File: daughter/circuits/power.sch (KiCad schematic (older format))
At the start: 44 parts, among them J5 Barrel_Jack_OD5.5_ID2.5, J6 Barrel_Jack_OD5.5_ID2.5, J7 Barrel_Jack_OD5.5_ID2.5, U2 LTV-827S, U3 ACS711, U4 REG_3V3, U5 MIC29302WU, U6 MIC29302WU, U7 MIC29302WU

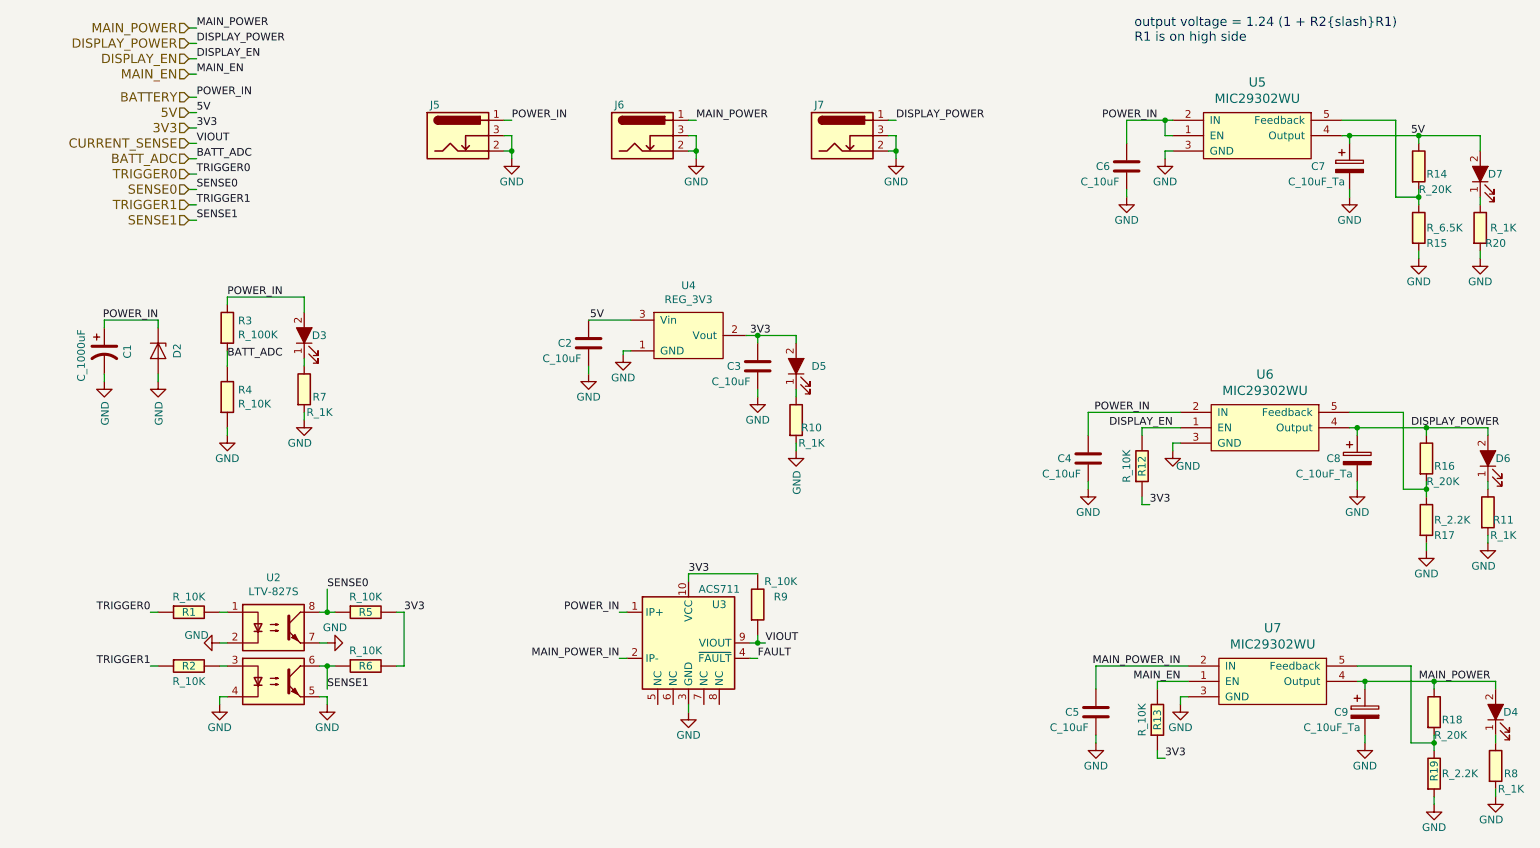
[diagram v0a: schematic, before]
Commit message: 0) Switched to h-bridge drivers for hvac 1) Connected ignition sense io 2) MCP config pins and reset 3) Fixed usb resistors 4) Fixed BJT footprint 5) Added car interface pcb for C6 Corvette
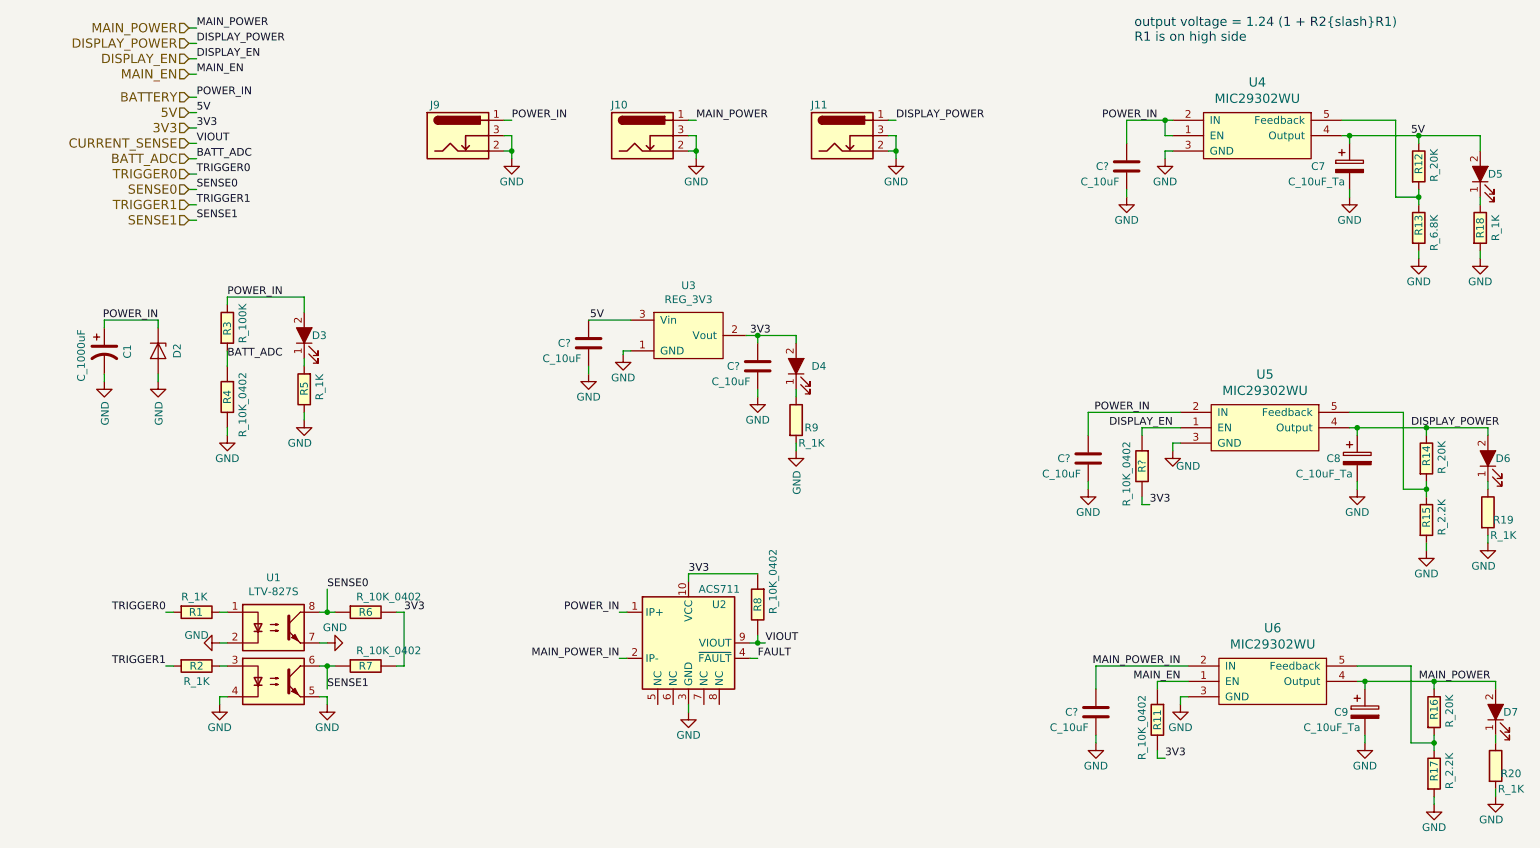
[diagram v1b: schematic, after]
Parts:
- removed C2, C3, C4, C5, C6: C_10uF, Capacitor_SMD:C_0603_1608Metric_Pad1.08x0.95mm_HandSolder, symbol open-dash-daughterboard-rescue:C_10uF-Open_Automation
- removed R1, R12, R13, R2, R4, R5, R6, R9: R_10K, Resistor_SMD:R_0603_1608Metric_Pad0.98x0.95mm_HandSolder, symbol open-dash-daughterboard-rescue:R_10K-Open_Automation
- removed R14, R16, R18: R_20K, Resistor_SMD:R_0603_1608Metric_Pad0.98x0.95mm_HandSolder, symbol open-dash-daughterboard-rescue:R_20K-Open_Automation
- removed R15: R_6.5K, Resistor_SMD:R_0603_1608Metric_Pad0.98x0.95mm_HandSolder, symbol open-dash-daughterboard-rescue:R_6.5K-Open_Automation
- removed R17, R19: R_2.2K, Resistor_SMD:R_0603_1608Metric_Pad0.98x0.95mm_HandSolder, symbol open-dash-daughterboard-rescue:R_2.2K-Open_Automation
- removed R3: R_100K, Resistor_SMD:R_0603_1608Metric_Pad0.98x0.95mm_HandSolder, symbol open-dash-daughterboard-rescue:R_100K-Open_Automation
- removed R7, R8: R_1K, Resistor_SMD:R_0603_1608Metric_Pad0.98x0.95mm_HandSolder, symbol open-dash-daughterboard-rescue:R_1K-Open_Automation
- removed U5: MIC29302WU, Package_TO_SOT_SMD:TO-263-5_TabPin3, symbol open-dash-daughterboard-rescue:MIC29302WU-Open_Automation
- added C? (x5): C_10uF, Capacitor_SMD:C_0805_2012Metric_Pad1.18x1.45mm_HandSolder, symbol Open_Automation:C_10uF
- added R1, R2, R5: R_1K, Resistor_SMD:R_0603_1608Metric_Pad0.98x0.95mm_HandSolder, symbol Open_Automation:R_1K
- added R11, R4, R6, R7, R8, R?: R_10K_0402, Resistor_SMD:R_0402_1005Metric_Pad0.72x0.64mm_HandSolder, symbol Open_Automation:R_10K_0402
- added R12, R14, R16: R_20K, Resistor_SMD:R_0402_1005Metric_Pad0.72x0.64mm_HandSolder, symbol Open_Automation:R_20K
- added R13: R_6.8K, Resistor_SMD:R_0603_1608Metric_Pad0.98x0.95mm_HandSolder, symbol Open_Automation:R_6.8K
- added R15, R17: R_2.2K, Resistor_SMD:R_0402_1005Metric_Pad0.72x0.64mm_HandSolder, symbol Open_Automation:R_2.2K
- added R20: R_1K, Resistor_SMD:R_0603_1608Metric_Pad0.98x0.95mm_HandSolder, symbol open-dash-daughterboard-rescue:R_1K-Open_Automation
- added R3: R_100K, Resistor_SMD:R_0603_1608Metric_Pad0.98x0.95mm_HandSolder, symbol Open_Automation:R_100K
- added U4: MIC29302WU, Package_TO_SOT_SMD:TO-263-5_TabPin3, symbol open-dash-daughterboard-rescue:MIC29302WU-Open_Automation
- renumbered D5 to D4, D7 to D5, D4 to D7, J6 to J10, J7 to J11, J5 to J9, R20 to R18, R11 to R19, R10 to R9, U2 to U1, U3 to U2, U4 to U3, U6 to U5, U7 to U6
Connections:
- net 3V3: now also C?.1, R11.2, R6.2, R7.2, R8.1, R?.2
- net 5V: now also C?.1, R12.1, U4.4 (Output)
- net BATTERY: now also C?.1, C?.1, R3.1, U4.1 (EN), U4.2 (IN)
- net BATT_ADC: now also R3.2, R4.1
- net CURRENT_SENSE: now also R8.2
- net DISPLAY_EN: now also R?.1
- net DISPLAY_POWER: now also R14.1
- net GND: now also C?.2, C?.2, C?.2, C?.2, C?.2, R13.2, R15.2, R17.2, R20.2, R4.2, R5.1, U4.3 (GND)
- net MAIN_EN: now also R11.1
- net MAIN_POWER: now also R16.1
- net MAIN_POWER_IN: now also C?.1
- net SENSE0: now also R6.1
- net SENSE1: now also R7.1
- net TRIGGER0: now also R1.2
- net TRIGGER1: now also R2.2
- net at U5.5 (Feedback): now also R14.2, R15.1
- net at U6.5 (Feedback): now also R16.2, R17.1
- net at D3.1 (K): now also R5.2
- net at D7.1 (K): now also R20.1
- net at U1.1: now also R1.1
- net at U1.3: now also R2.1
- new net: R12.2, R13.1, U4.5 (Feedback)

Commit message: finished schematic, working on layout
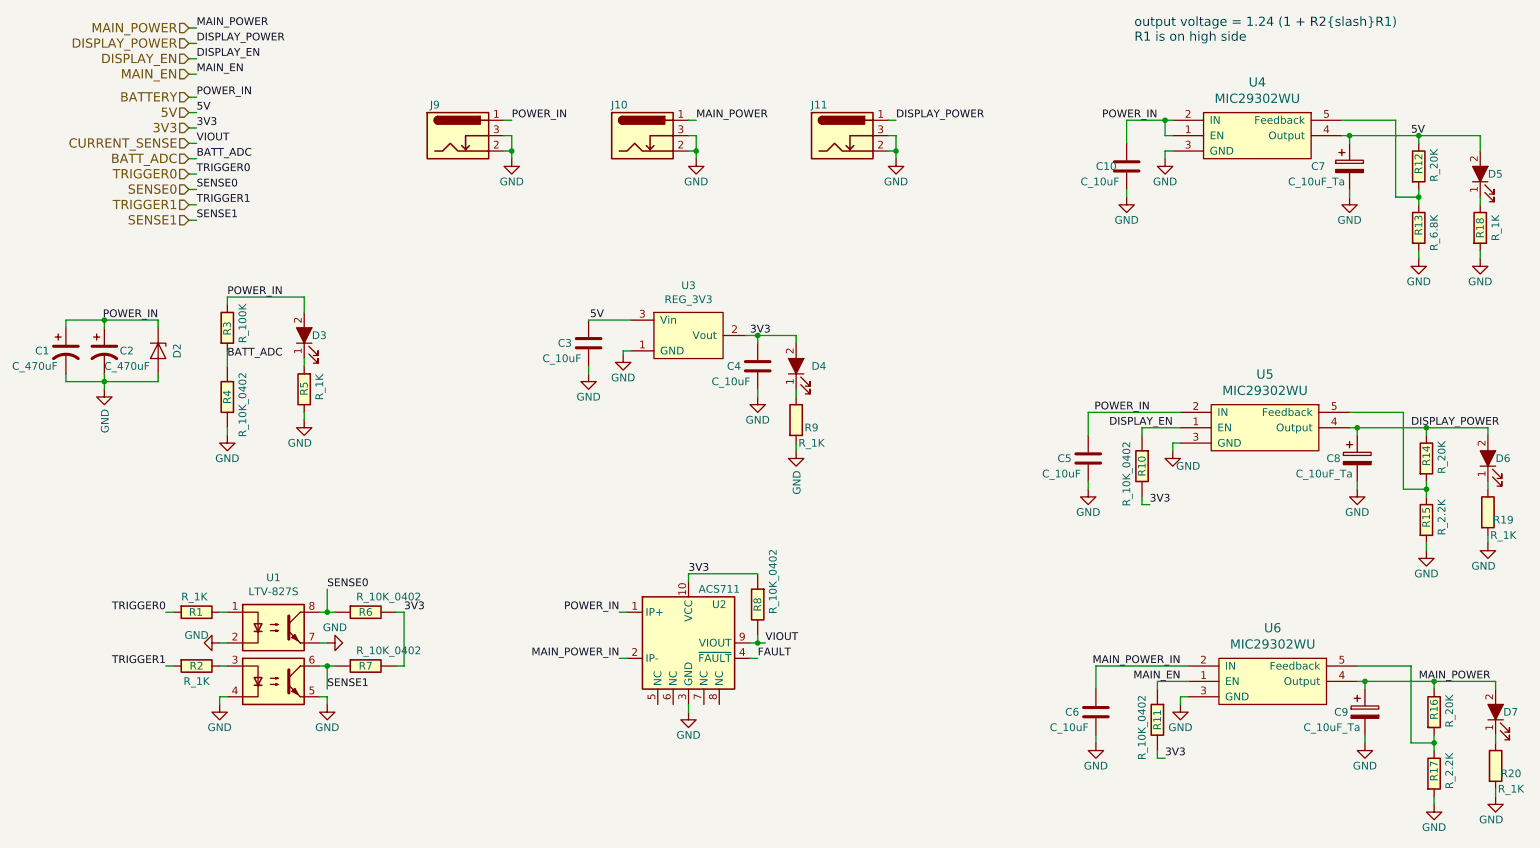
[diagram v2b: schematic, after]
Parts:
- removed C1: C_1000uF, Capacitor_THT:CP_Radial_D12.5mm_P5.00mm, symbol open-dash-daughterboard-rescue:C_1000uF-Open_Automation
- added C1, C2: C_470uF, Capacitor_SMD:CP_Elec_10x10, symbol Open_Automation:C_470uF
- gave numbers to parts that had none: 6
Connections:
- net BATTERY: now also C1.1, C2.1
- net GND: now also C1.2, C2.2
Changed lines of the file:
@@
 L open-dash-daughterboard-rescue:GND-power #PWR025
 U 1 1 5FD22FE0
-P 1150 3350
-F 0 "#PWR025" H 1150 3100 50  0001 C CNN
-F 1 "GND" V 1155 3222 50  0000 R CNN
-F 2 "" H 1150 3350 50  0001 C CNN
-F 3 "" H 1150 3350 50  0001 C CNN
-	1    1150 3350
-	1    0    0    -1
-$EndComp
-$Comp
-L open-dash-daughterboard-rescue:GND-power #PWR026
-U 1 1 5FD22FD6
-P 1500 3350
-F 0 "#PWR026" H 1500 3100 50  0001 C CNN
-F 1 "GND" V 1505 3222 50  0000 R CNN
-F 2 "" H 1500 3350 50  0001 C CNN
-F 3 "" H 1500 3350 50  0001 C CNN
-	1    1500 3350
+P 1150 3400
+F 0 "#PWR025" H 1150 3150 50  0001 C CNN
+F 1 "GND" V 1155 3272 50  0000 R CNN
+F 2 "" H 1150 3400 50  0001 C CNN
+F 3 "" H 1150 3400 50  0001 C CNN
+	1    1150 3400
 	1    0    0    -1
 $EndComp
@@
 F 3 "" H 4525 3175 50  0000 C CNN
 	1    4525 3175
-	1    0    0    -1
-$EndComp
-$Comp
-L open-dash-daughterboard-rescue:C_1000uF-Open_Automation C?
-U 1 1 5CC3872E
-P 1150 3150
-AR Path="/5ABD18ED/5CC3872E" Ref="C?"  Part="1"
-AR Path="/5CC3872E" Ref="C?"  Part="1"
-AR Path="/5A7BADB8/5CC3872E" Ref="C1"  Part="1"
-F 0 "C1" V 1300 3100 50  0000 L CNN
-F 1 "C_1000uF" V 1000 2950 50  0000 L CNN
-F 2 "Capacitor_THT:CP_Radial_D12.5mm_P5.00mm" H 1250 3450 50  0001 C CNN
-F 3 "https://industrial.panasonic.com/ww/products/capacitors/aluminum-capacitors/aluminum-cap-lead/fc/EEUFC1E102" H 1150 2900 50  0001 C CNN
-F 4 " EEU-FC1E102" H 1275 3350 60  0001 C CNN "Part Number"
-	1    1150 3150
 	1    0    0    -1
 $EndComp
@@
 $EndComp
 $Comp
-L Open_Automation:C_10uF C?
+L Open_Automation:C_10uF C3
 U 1 1 60502A0A
 P 4300 3100
-F 0 "C?" H 4100 3100 50  0000 L CNN
+F 0 "C3" H 4100 3100 50  0000 L CNN
 F 1 "C_10uF" H 4000 3000 50  0000 L CNN
 F 2 "Capacitor_SMD:C_0805_2012Metric_Pad1.18x1.45mm_HandSolder" H 4550 3550 50  0001 C CNN
@@
 $EndComp
 $Comp
-L Open_Automation:C_10uF C?
+L Open_Automation:C_10uF C4
 U 1 1 605049B8
 P 5400 3250
-F 0 "C?" H 5200 3250 50  0000 L CNN
+F 0 "C4" H 5200 3250 50  0000 L CNN
 F 1 "C_10uF" H 5100 3150 50  0000 L CNN
 F 2 "Capacitor_SMD:C_0805_2012Metric_Pad1.18x1.45mm_HandSolder" H 5650 3700 50  0001 C CNN
@@
 $EndComp
 $Comp
-L Open_Automation:C_10uF C?
+L Open_Automation:C_10uF C10
 U 1 1 605052BC
 P 7800 1950
-F 0 "C?" H 7600 1950 50  0000 L CNN
+F 0 "C10" H 7600 1950 50  0000 L CNN
 F 1 "C_10uF" H 7500 1850 50  0000 L CNN
 F 2 "Capacitor_SMD:C_0805_2012Metric_Pad1.18x1.45mm_HandSolder" H 8050 2400 50  0001 C CNN
@@
 $EndComp
 $Comp
-L Open_Automation:C_10uF C?
+L Open_Automation:C_10uF C5
 U 1 1 60506FE4
 P 7550 3850
-F 0 "C?" H 7350 3850 50  0000 L CNN
+F 0 "C5" H 7350 3850 50  0000 L CNN
 F 1 "C_10uF" H 7250 3750 50  0000 L CNN
 F 2 "Capacitor_SMD:C_0805_2012Metric_Pad1.18x1.45mm_HandSolder" H 7800 4300 50  0001 C CNN
@@
 $EndComp
 $Comp
-L Open_Automation:C_10uF C?
+L Open_Automation:C_10uF C6
 U 1 1 605088D7
 P 7600 5500
-F 0 "C?" H 7400 5500 50  0000 L CNN
+F 0 "C6" H 7400 5500 50  0000 L CNN
 F 1 "C_10uF" H 7300 5400 50  0000 L CNN
 F 2 "Capacitor_SMD:C_0805_2012Metric_Pad1.18x1.45mm_HandSolder" H 7850 5950 50  0001 C CNN
@@
 $EndComp
 $Comp
-L Open_Automation:R_10K_0402 R?
+L Open_Automation:R_10K_0402 R10
 U 1 1 605484A2
 P 7900 3900
-F 0 "R?" V 7900 3900 50  0000 C CNN
+F 0 "R10" V 7900 3900 50  0000 C CNN
 F 1 "R_10K_0402" V 8000 3950 50  0000 C CNN
 F 2 "Resistor_SMD:R_0402_1005Metric_Pad0.72x0.64mm_HandSolder" V 7830 3900 50  0001 C CNN
@@
 	-1   0    0    1
 $EndComp
+$Comp
+L Open_Automation:C_470uF C2
+U 1 1 604A9AA4
+P 1150 3150
+F 0 "C2" H 1250 3150 50  0000 L CNN
+F 1 "C_470uF" H 1150 3050 50  0000 L CNN
+F 2 "Capacitor_SMD:CP_Elec_10x10" H 1150 3150 50  0001 C CNN
+F 3 "https://datasheet.lcsc.com/szlcsc/1809192324_Honor-Elec-RVT1V471M1010_C3350.pdf" H 1150 3150 50  0001 C CNN
+F 4 "RVT1V471M1010" H 1150 3150 50  0001 C CNN "Part Number"
+F 5 "C3350" H 1150 3150 50  0001 C CNN "LCSC"
+	1    1150 3150
+	1    0    0    -1
+$EndComp
+$Comp
+L Open_Automation:C_470uF C1
+U 1 1 604AC15F
+P 900 3150
+F 0 "C1" H 700 3150 50  0000 L CNN
+F 1 "C_470uF" H 550 3050 50  0000 L CNN
+F 2 "Capacitor_SMD:CP_Elec_10x10" H 900 3150 50  0001 C CNN
+F 3 "https://datasheet.lcsc.com/szlcsc/1809192324_Honor-Elec-RVT1V471M1010_C3350.pdf" H 900 3150 50  0001 C CNN
+F 4 "RVT1V471M1010" H 900 3150 50  0001 C CNN "Part Number"
+F 5 "C3350" H 900 3150 50  0001 C CNN "LCSC"
+	1    900  3150
+	1    0    0    -1
+$EndComp
+Wire Wire Line
+	900  3000 900  2950
+Wire Wire Line
+	900  2950 1150 2950
+Connection ~ 1150 2950
+Wire Wire Line
+	900  3300 900  3350
+Wire Wire Line
+	900  3350 1150 3350
+Connection ~ 1150 3350
+Wire Wire Line
+	1500 3350 1150 3350
+Wire Wire Line
+	1150 3400 1150 3350
 $EndSCHEMATC

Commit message: sent v1.2 to fab
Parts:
- removed R8: R_10K_0402, Resistor_SMD:R_0402_1005Metric_Pad0.72x0.64mm_HandSolder, symbol Open_Automation:R_10K_0402
- removed U1: LTV-827S, Package_DIP:SMDIP-8_W9.53mm, symbol open-dash-daughterboard-rescue:LTV-827S-Open_Automation
- removed U2: ACS711, Sensor_Current:Allegro_QFN-12-10-1EP_3x3mm_P0.5mm, symbol open-dash-daughterboard-rescue:ACS711-Open_Automation
- removed U3: REG_3V3, Package_TO_SOT_SMD:TO-252-2, symbol open-dash-daughterboard-rescue:REG_3V3-Open_Automation
- added C37: C_1nF_0402, Capacitor_SMD:C_0402_1005Metric_Pad0.74x0.62mm_HandSolder, symbol Open_Automation:C_1nF_0402
- added U1: Opto_TLP521, Package_DIP:SMDIP-8_W9.53mm, symbol Open_Automation:Opto_TLP521
- added U11: REG_AMS1117-3.3, Package_TO_SOT_SMD:SOT-223-3_TabPin2, symbol Open_Automation:REG_AMS1117-3.3
- added U2: ACS711, Package_SO:SOIC-8_3.9x4.9mm_P1.27mm, symbol Open_Automation:ACS711
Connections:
- net 3V3: now also U11.2 (Vout)
- net 5V: now also U11.3 (Vin), U2.8 (VCC)
- net BATTERY: now also U2.1 (IP+), U2.2 (IP+)
- net CURRENT_SENSE: now also U2.7 (VIOUT)
- net GND: now also C37.2, U1.2, U1.4, U1.5, U1.7, U11.1 (GND), U2.5 (GND)
- net MAIN_POWER_IN: now also U2.3 (IP-), U2.4 (IP-)
- net SENSE0: now also U1.8
- net SENSE1: now also U1.6
- net at R1.1: now also U1.1
- net at R2.1: now also U1.3
- new net: C37.1, U2.6 (FILTER)
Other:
- moved on the sheet: C4, D4, R9

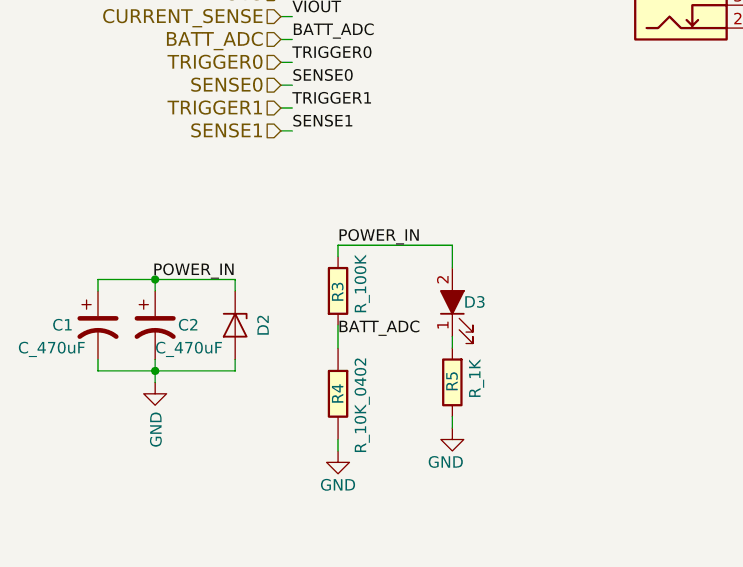
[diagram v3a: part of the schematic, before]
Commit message: Added external amp trigger code and circuit to PCB. Made some layout modifications.
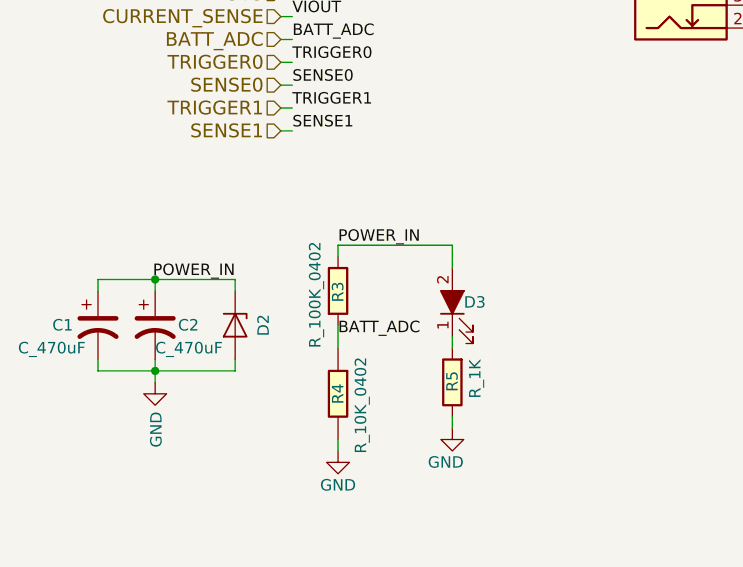
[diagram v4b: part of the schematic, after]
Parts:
- removed R3: R_100K, Resistor_SMD:R_0603_1608Metric_Pad0.98x0.95mm_HandSolder, symbol Open_Automation:R_100K
- added R3: R_100K_0402, Resistor_SMD:R_0402_1005Metric_Pad0.72x0.64mm_HandSolder, symbol Open_Automation:R_100K_0402
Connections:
- net BATTERY: now also R3.1
- net BATT_ADC: now also R3.2
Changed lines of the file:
@@
-$EndComp
-$Comp
-L Open_Automation:R_100K R3
-U 1 1 6044C59E
-P 1950 3000
-F 0 "R3" V 1950 2950 50  0000 L CNN
-F 1 "R_100K" V 2050 2900 50  0000 L CNN
-F 2 "Resistor_SMD:R_0603_1608Metric_Pad0.98x0.95mm_HandSolder" V 1880 3000 50  0001 C CNN
-F 3 "https://datasheet.lcsc.com/szlcsc/Uniroyal-Elec-0603WAF1003T5E_C25803.pdf" V 2030 3000 50  0001 C CNN
-F 4 "0603WAF1003T5E" V 2130 3100 60  0001 C CNN "Part Number"
-F 5 "C25803" V 1800 3000 50  0001 C CNN "LCSC"
-	1    1950 3000
-	1    0    0    -1
 $EndComp
 $Comp
@@
 	1    0    0    -1
 $EndComp
+$Comp
+L Open_Automation:R_100K_0402 R3
+U 1 1 61AC8D3E
+P 1950 3000
+F 0 "R3" V 1950 2950 50  0000 L CNN
+F 1 "R_100K_0402" V 1850 2750 50  0000 L CNN
+F 2 "Resistor_SMD:R_0402_1005Metric_Pad0.72x0.64mm_HandSolder" V 1880 3000 50  0001 C CNN
+F 3 "https://datasheet.lcsc.com/lcsc/1810111814_UNI-ROYAL-Uniroyal-Elec-0402WGF1003TCE_C25741.pdf" V 2030 3000 50  0001 C CNN
+F 4 "0402WGF1003TCE" V 2130 3100 60  0001 C CNN "Part Number"
+F 5 "C25741" V 1800 3000 50  0001 C CNN "LCSC"
+	1    1950 3000
+	1    0    0    -1
+$EndComp
